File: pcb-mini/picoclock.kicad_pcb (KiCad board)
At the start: 4 copper layers, 140 x 54 mm, 143 parts, among them J1 UART, J10 USB, J11 Alt Power, J12 LED_5V, J13 ESP32_IO0, J14 SJ2-35863B1-SMT-TR, J15 Conn_01x24, J2 USB_A, J3 UART, J4 xx, J5 Micro_SD_Card_Det1, J6 USB_C_Receptacle, J8 Conn_01x21_Pin, J9 AUDIO, Q1 BSS138, Q3 BSS138, SW1 SW_Push, SW2 SW_Push, SW3 SW_Push, SW4 SW_Push, SW5 SW_Push, SW6 SW_Push, SW7 SW_Push, U1 PCF8563T, U10 74LS157, U12 ENS160, U13 TCR2EE19, U2 RP2350_80QFN, U3 MCP9808_MSOP, U4 PCM5100, U5 PAM8302A, U6 W25Q128JVS, U7 MCP45X1-104E, U8 NCP1117-3.3_SOT223, U9 ESP32-WROOM-E, Y1 Crystal, Y2 ABM8-272-T3

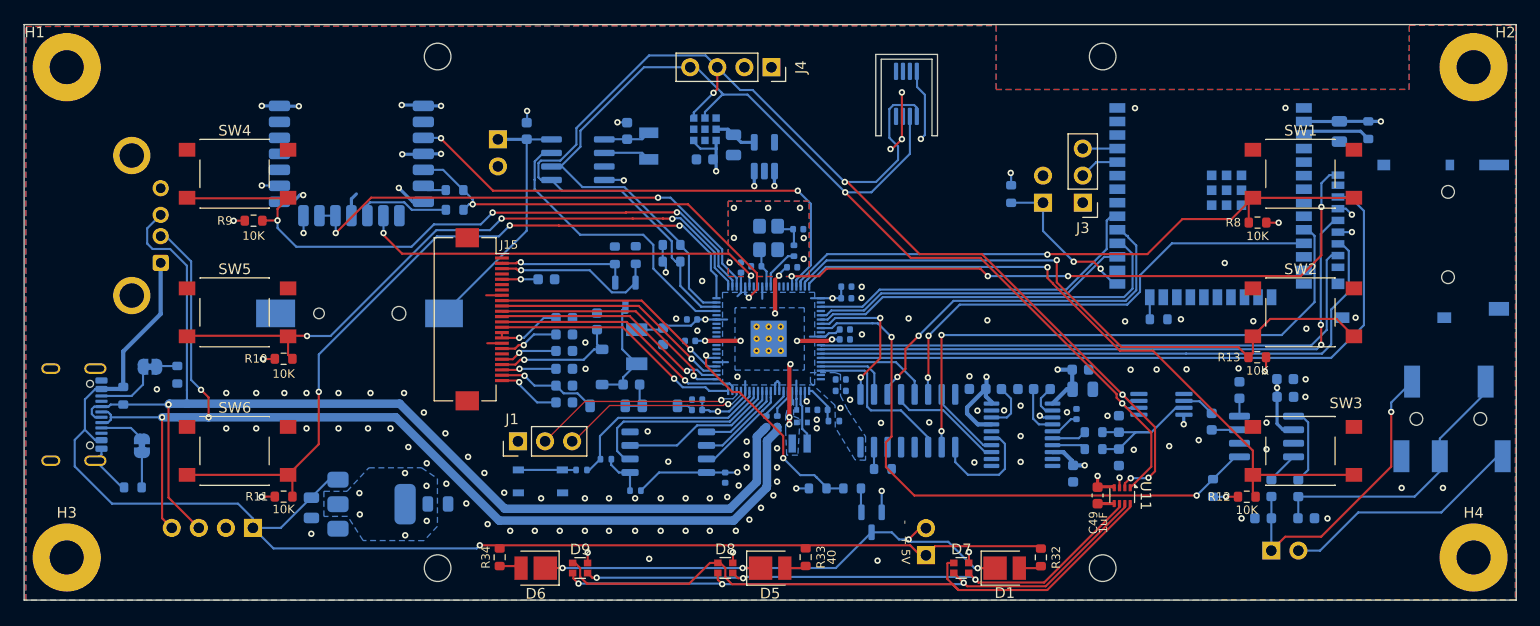
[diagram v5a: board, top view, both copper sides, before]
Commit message: [pcb] mini: add debug port, improve/fix traces
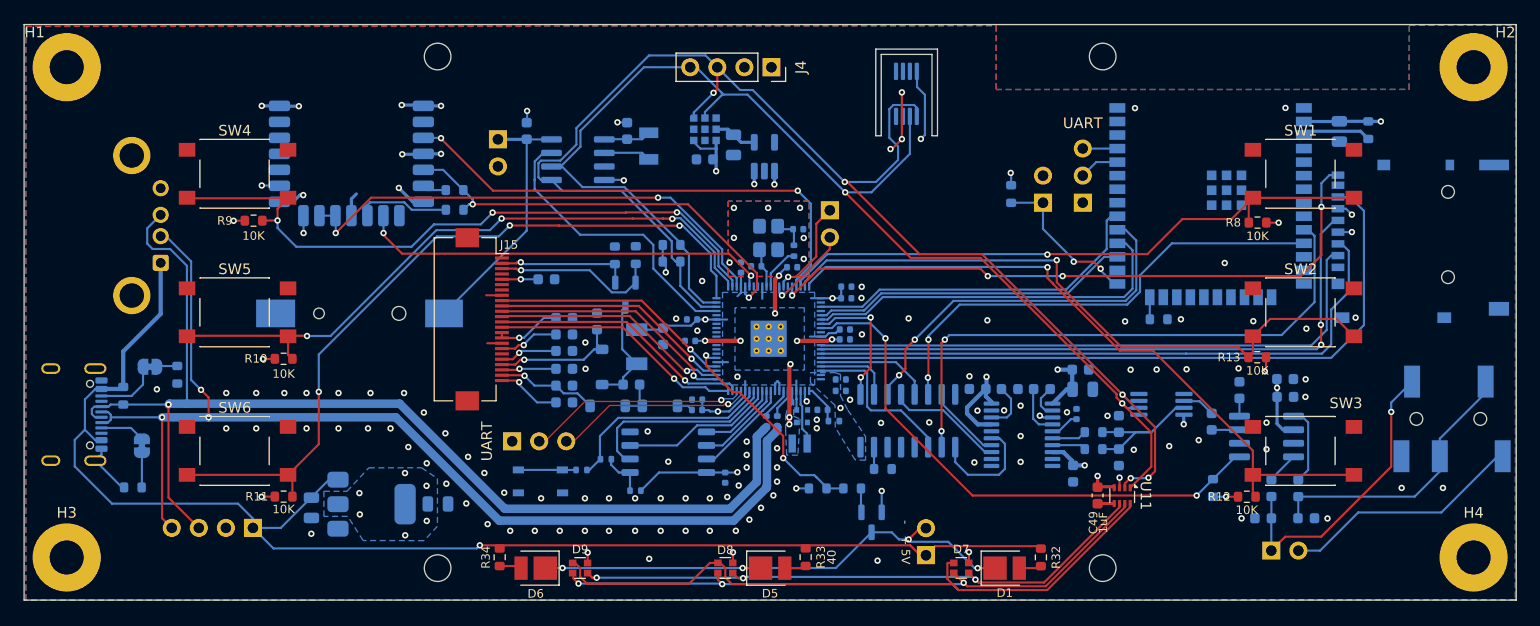
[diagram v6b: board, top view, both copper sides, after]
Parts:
- added J7: DBG, Connector_PinHeader_2.54mm:PinHeader_1x02_P2.54mm_Vertical, B.Cu at (155.6, 97.4)
- J1, J3: moved to B.Cu
- moved J1 0.55 mm to (125.8, 119.1), turned to -90 degrees
- turned J3 to 0 degrees
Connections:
- U2 pad 33: /uC/SWCLK -> SWCLK
- U2 pad 34: /uC/SWD -> SWD
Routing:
- net SWD: track 0.00 -> 9.38 mm, vias 0 -> 1
- net SWCLK: track 0.00 -> 8.33 mm, vias 0 -> 1
- net MUTE: track 55.6 -> 51.5 mm
- net GPIO35_I2S_SELECT: track 13.8 -> 12.6 mm
- net GPIO0_TX: track 18.0 -> 19.1 mm
- net SD_DET: track 60.7 -> 61.3 mm
- net GPIO1_RX: track 20.2 -> 20.7 mm
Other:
- outline, holes or cut-outs redrawn
- board text added: "IO0"
- board text added: "SWCLK"
- board text added: "SWD"
